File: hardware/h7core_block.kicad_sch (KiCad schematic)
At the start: 71 parts, among them J1 USB-C, J3 TC2030-NL SWD, U1 STM32H743VIT6, U3 AP63203WU-7, U4 TLV75533PDBVR, U6 PCM5102APWR, U8 PCM1808PWR, Y1 25MHz 12pF

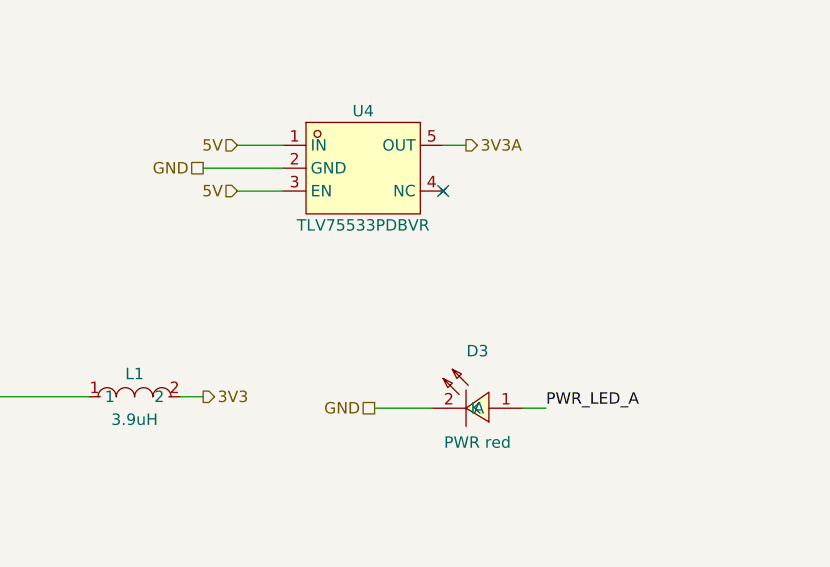
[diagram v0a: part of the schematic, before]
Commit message: feat(sch): add SP809 3V3 supervisor gating TLV75533 EN
U107 SP809EK-L-2-9 (push-pull active-low, 2.9 V, 140 ms min) drives TLV75533 EN on new net LDO_EN, replacing the 5V tie, so 3V3A comes up only after 3V3 is valid. C166 100 nF at its VCC. No pull-up: the output is push-pull.
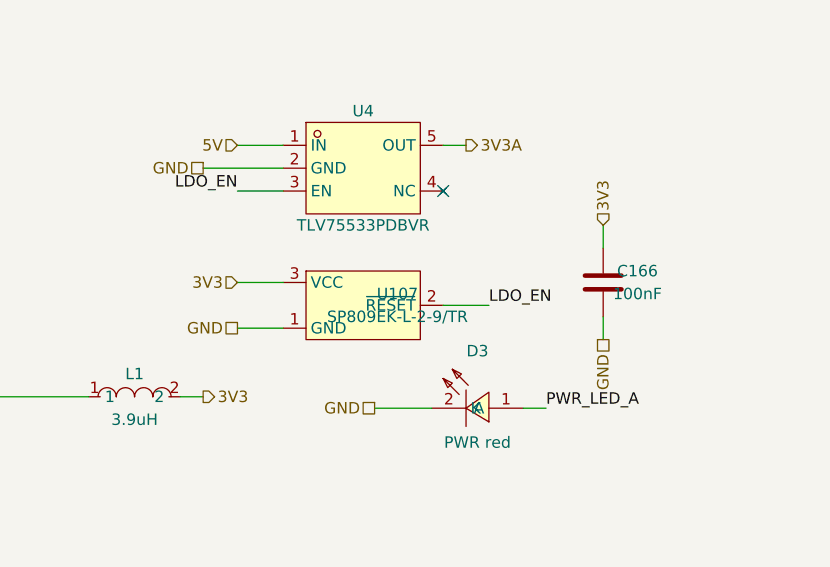
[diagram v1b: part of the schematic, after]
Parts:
- added C166: 100nF, Capacitor_SMD:C_0402_1005Metric, symbol Device:C
- added U107: SP809EK-L-2-9/TR, Package_TO_SOT_SMD:SOT-23, symbol cubevox_h7core:SP809EK-L-2-9
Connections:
- net 3V3: now also C166.1, U107.3 (VCC)
- net 5V: no longer U4.3 (EN)
- net GND: now also C166.2, U107.1 (GND)
- new net LDO_EN: U107.2 (~{RESET}), U4.3 (EN)
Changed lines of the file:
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@@
 		)
 	)
-	(hierarchical_label "5V"
-		(shape input)
+	(label "LDO_EN"
 		(at 284.48 104.14 180)
 		(fields_autoplaced yes)
@@
 		)
 	)
+	(symbol
+		(lib_id "cubevox_h7core:SP809EK-L-2-9")
+		(at 298.45 116.84 0)
+		(unit 1)
+		(exclude_from_sim no)
+		(in_bom yes)
+		(on_board yes)
+		(dnp no)
+		(property "Reference" "U107"
+			(at 302.26 115.57000000000001 0)
+			(effects
+				(font
+					(size 1.27 1.27)
+				)
+			)
+		)
+		(property "Value" "SP809EK-L-2-9/TR"
+			(at 302.26 118.11 0)
+			(effects
+				(font
+					(size 1.27 1.27)
+				)
+			)
+		)
+		(property "Footprint" "Package_TO_SOT_SMD:SOT-23"
+			(at 298.45 116.84 0)
+			(hide yes)
+			(effects
+				(font
+					(size 1.27 1.27)
+				)
+			)
+		)
+		(property "Datasheet" "~"
+			(at 298.45 116.84 0)
+			(hide yes)
+			(effects
+				(font
+					(size 1.27 1.27)
+				)
+			)
+		)
+		(property "LCSC" "C412495"
+			(at 298.45 116.84 0)
+			(hide yes)
+			(effects
+				(font
+					(size 1.27 1.27)
+				)
+			)
+		)
+		(property "MPN" "SP809EK-L-2-9/TR"
+			(at 298.45 116.84 0)
+			(hide yes)
+			(effects
+				(font
+					(size 1.27 1.27)
+				)
+			)
+		)
+		(pin "1"
+		)
+		(pin "2"
+		)
+		(pin "3"
+		)
+		(instances
+			(project "cubevox"
+				(path "/99ad1494-2bf8-5051-8886-2c8b83c86254/cdf9c81d-d554-530c-ae51-0929232e7fb3"
+					(reference "U107")
+					(unit 1)
+				)
+			)
+		)
+	)
+	(wire
+		(pts
+			(xy 289.56 114.3) (xy 284.48 114.3)
+		)
+		(stroke
+			(width 0)
+			(type default)
+		)
+	)
+	(hierarchical_label "3V3"
+		(shape input)
+		(at 284.48 114.3 180)
+		(fields_autoplaced yes)
+		(effects
+			(font
+				(size 1.27 1.27)
+			)
+			(justify right bottom)
+		)
+	)
+	(wire
+		(pts
+			(xy 289.56 119.38) (xy 284.48 119.38)
+		)
+		(stroke
+			(width 0)
+			(type default)
+		)
+	)
+	(hierarchical_label "GND"
+		(shape passive)
+		(at 284.48 119.38 180)
+		(fields_autoplaced yes)
+		(effects
+			(font
+				(size 1.27 1.27)
+			)
+			(justify right bottom)
+		)
+	)
+	(wire
+		(pts
+			(xy 307.34 116.84) (xy 312.42 116.84)
+		)
+		(stroke
+			(width 0)
+			(type default)
+		)
+	)
+	(label "LDO_EN"
+		(at 312.42 116.84 0)
+		(fields_autoplaced yes)
+		(effects
+			(font
+				(size 1.27 1.27)
+			)
+			(justify left bottom)
+		)
+	)
+	(symbol
+		(lib_id "Device:C")
+		(at 325.12 114.3 0)
+		(unit 1)
+		(exclude_from_sim no)
+		(in_bom yes)
+		(on_board yes)
+		(dnp no)
+		(property "Reference" "C166"
+			(at 328.93 113.03 0)
+			(effects
+				(font
+					(size 1.27 1.27)
+				)
+			)
+		)
+		(property "Value" "100nF"
+			(at 328.93 115.57 0)
+			(effects
+				(font
+					(size 1.27 1.27)
+				)
+			)
+		)
+		(property "Footprint" "Capacitor_SMD:C_0402_1005Metric"
+			(at 325.12 114.3 0)
+			(hide yes)
+			(effects
+				(font
+					(size 1.27 1.27)
+				)
+			)
+		)
+		(property "Datasheet" "~"
+			(at 325.12 114.3 0)
+			(hide yes)
+			(effects
+				(font
+					(size 1.27 1.27)
+				)
+			)
+		)
+		(property "LCSC" "C1525"
+			(at 325.12 114.3 0)
+			(hide yes)
+			(effects
+				(font
+					(size 1.27 1.27)
+				)
+			)
+		)
+		(pin "1"
+		)
+		(pin "2"
+		)
+		(instances
+			(project "cubevox"
+				(path "/99ad1494-2bf8-5051-8886-2c8b83c86254/cdf9c81d-d554-530c-ae51-0929232e7fb3"
+					(reference "C166")
+					(unit 1)
+				)
+			)
+		)
+	)
+	(wire
+		(pts
+			(xy 325.12 110.49) (xy 325.12 107.95)
+		)
+		(stroke
+			(width 0)
+			(type default)
+		)
+	)
+	(hierarchical_label "3V3"
+		(shape input)
+		(at 325.12 107.95 90)
+		(fields_autoplaced yes)
+		(effects
+			(font
+				(size 1.27 1.27)
+			)
+			(justify left bottom)
+		)
+	)
+	(wire
+		(pts
+			(xy 325.12 118.11) (xy 325.12 120.64999999999999)
+		)
+		(stroke
+			(width 0)
+			(type default)
+		)
+	)
+	(hierarchical_label "GND"
+		(shape passive)
+		(at 325.12 120.64999999999999 270)
+		(fields_autoplaced yes)
+		(effects
+			(font
+				(size 1.27 1.27)
+			)
+			(justify right bottom)
+		)
+	)

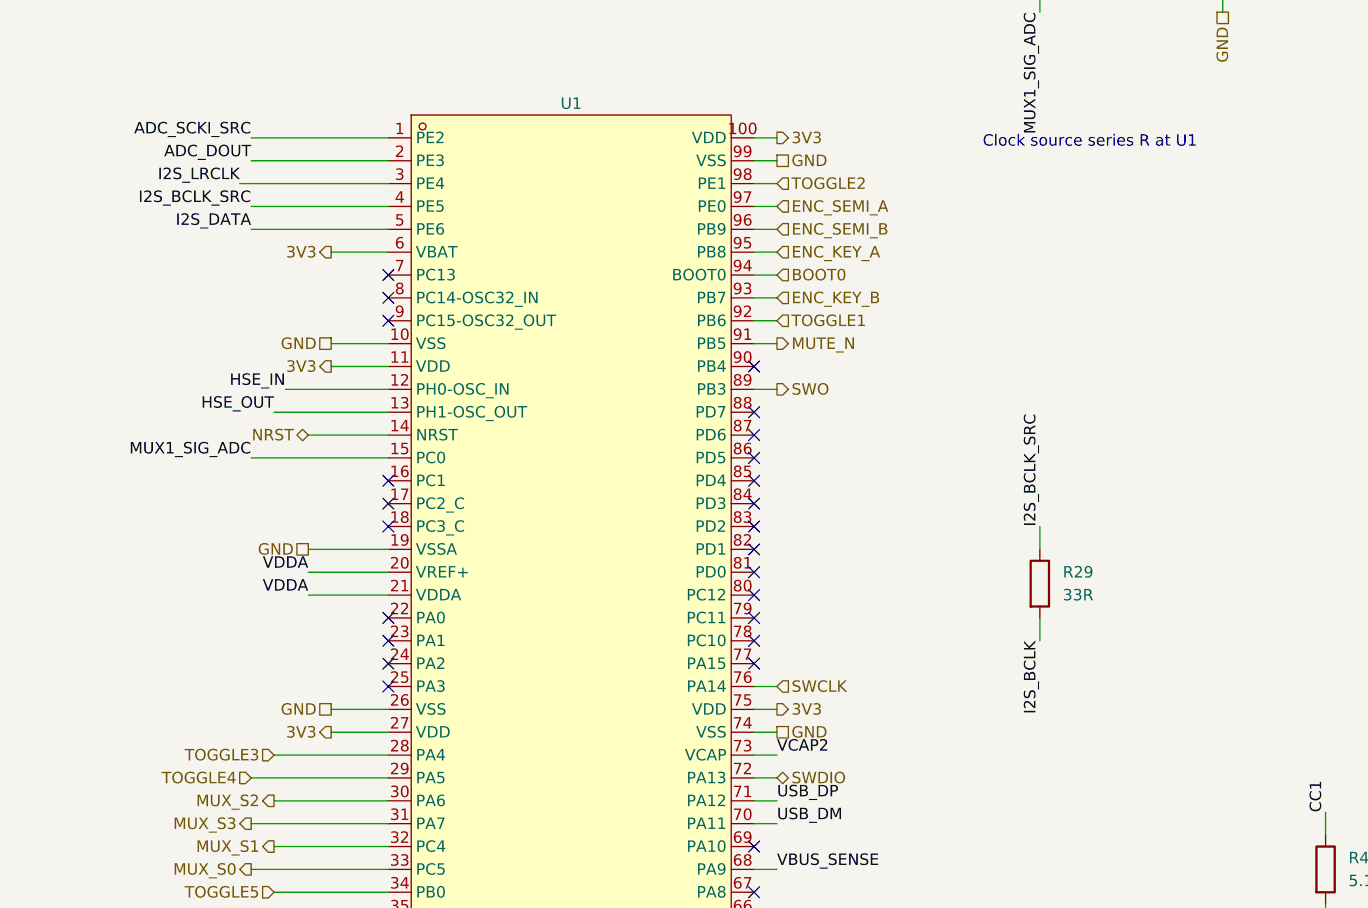
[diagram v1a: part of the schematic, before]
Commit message: feat(sch): add 33R series resistors on I2S at U1
R156 (LRCLK) and R157 (DATA), 33R 0402 (LCSC C25105), sit at the U1 escapes like R29 on BCLK, so each I2S line leaves the MCU through a source resistor. U1 sides become I2S_LRCLK_SRC and I2S_DATA_SRC. ERC: no new violations.
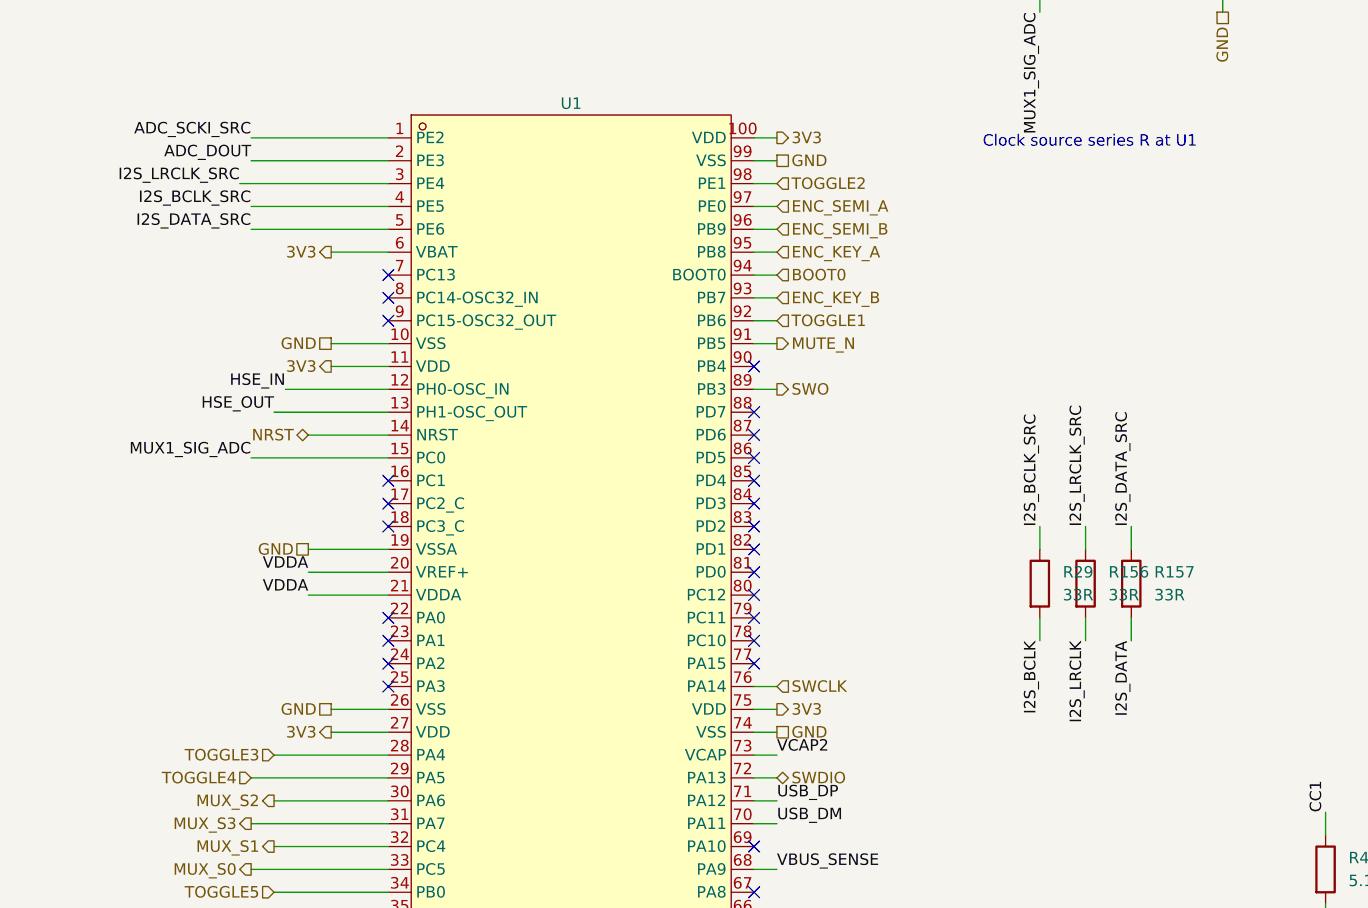
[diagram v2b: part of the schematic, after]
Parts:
- added R156, R157: 33R, Resistor_SMD:R_0402_1005Metric, symbol Device:R
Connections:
- net I2S_DATA: now also R157.2; no longer U1.5 (PE6)
- net I2S_LRCLK: now also R156.2; no longer U1.3 (PE4)
- new net I2S_DATA_SRC: R157.1, U1.5 (PE6)
- new net I2S_LRCLK_SRC: R156.1, U1.3 (PE4)
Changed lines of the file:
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@@
 		)
 	)
-	(label "I2S_LRCLK"
+	(label "I2S_LRCLK_SRC"
 		(at 38.1 82.55 180)
 		(fields_autoplaced yes)
@@
 		)
 	)
-	(label "I2S_DATA"
+	(label "I2S_DATA_SRC"
 		(at 39.37 87.63 180)
 		(fields_autoplaced yes)
@@
 		(fields_autoplaced yes)
 		(effects
+			(font
+				(size 1.27 1.27)
+			)
+			(justify right bottom)
+		)
+	)
+	(symbol
+		(lib_id "Device:R")
+		(at 132.08 127 0)
+		(unit 1)
+		(exclude_from_sim no)
+		(in_bom yes)
+		(on_board yes)
+		(dnp no)
+		(property "Reference" "R156"
+			(at 134.62 125.73 0)
+			(effects
+				(font
+					(size 1.27 1.27)
+				)
+				(justify left)
+			)
+		)
+		(property "Value" "33R"
+			(at 134.62 128.27 0)
+			(effects
+				(font
+					(size 1.27 1.27)
+				)
+				(justify left)
+			)
+		)
+		(property "Footprint" "Resistor_SMD:R_0402_1005Metric"
+			(at 132.08 127 0)
+			(hide yes)
+			(effects
+				(font
+					(size 1.27 1.27)
+				)
+			)
+		)
+		(property "Datasheet" "~"
+			(at 132.08 127 0)
+			(hide yes)
+			(effects
+				(font
+					(size 1.27 1.27)
+				)
+			)
+		)
+		(property "LCSC" "C25105"
+			(at 132.08 127 0)
+			(hide yes)
+			(effects
+				(font
+					(size 1.27 1.27)
+				)
+			)
+		)
+		(pin "1"
+		)
+		(pin "2"
+		)
+		(instances
+			(project "cubevox"
+				(path "/99ad1494-2bf8-5051-8886-2c8b83c86254/cdf9c81d-d554-530c-ae51-0929232e7fb3"
+					(reference "R156")
+					(unit 1)
+				)
+			)
+		)
+	)
+	(wire
+		(pts
+			(xy 132.08 123.19) (xy 132.08 120.65)
+		)
+		(stroke
+			(width 0)
+			(type default)
+		)
+	)
+	(label "I2S_LRCLK_SRC"
+		(at 132.08 120.65 90)
+		(fields_autoplaced yes)
+		(effects
+			(font
+				(size 1.27 1.27)
+			)
+			(justify left bottom)
+		)
+	)
+	(wire
+		(pts
+			(xy 132.08 130.81) (xy 132.08 133.35)
+		)
+		(stroke
+			(width 0)
+			(type default)
+		)
+	)
+	(label "I2S_LRCLK"
+		(at 132.08 133.35 270)
+		(fields_autoplaced yes)
+		(effects
+			(font
+				(size 1.27 1.27)
+			)
+			(justify right bottom)
+		)
+	)
+	(symbol
+		(lib_id "Device:R")
+		(at 137.16 127 0)
+		(unit 1)
+		(exclude_from_sim no)
+		(in_bom yes)
+		(on_board yes)
+		(dnp no)
+		(property "Reference" "R157"
+			(at 139.7 125.73 0)
+			(effects
+				(font
+					(size 1.27 1.27)
+				)
+				(justify left)
+			)
+		)
+		(property "Value" "33R"
+			(at 139.7 128.27 0)
+			(effects
+				(font
+					(size 1.27 1.27)
+				)
+				(justify left)
+			)
+		)
+		(property "Footprint" "Resistor_SMD:R_0402_1005Metric"
+			(at 137.16 127 0)
+			(hide yes)
+			(effects
+				(font
+					(size 1.27 1.27)
+				)
+			)
+		)
+		(property "Datasheet" "~"
+			(at 137.16 127 0)
+			(hide yes)
+			(effects
+				(font
+					(size 1.27 1.27)
+				)
+			)
+		)
+		(property "LCSC" "C25105"
+			(at 137.16 127 0)
+			(hide yes)
+			(effects
+				(font
+					(size 1.27 1.27)
+				)
+			)
+		)
+		(pin "1"
+		)
+		(pin "2"
+		)
+		(instances
+			(project "cubevox"
+				(path "/99ad1494-2bf8-5051-8886-2c8b83c86254/cdf9c81d-d554-530c-ae51-0929232e7fb3"
+					(reference "R157")
+					(unit 1)
+				)
+			)
+		)
+	)
+	(wire
+		(pts
+			(xy 137.16 123.19) (xy 137.16 120.65)
+		)
+		(stroke
+			(width 0)
+			(type default)
+		)
+	)
+	(label "I2S_DATA_SRC"
+		(at 137.16 120.65 90)
+		(fields_autoplaced yes)
+		(effects
+			(font
+				(size 1.27 1.27)
+			)
+			(justify left bottom)
+		)
+	)
+	(wire
+		(pts
+			(xy 137.16 130.81) (xy 137.16 133.35)
+		)
+		(stroke
+			(width 0)
+			(type default)
+		)
+	)
+	(label "I2S_DATA"
+		(at 137.16 133.35 270)
+		(fields_autoplaced yes)
+		(effects

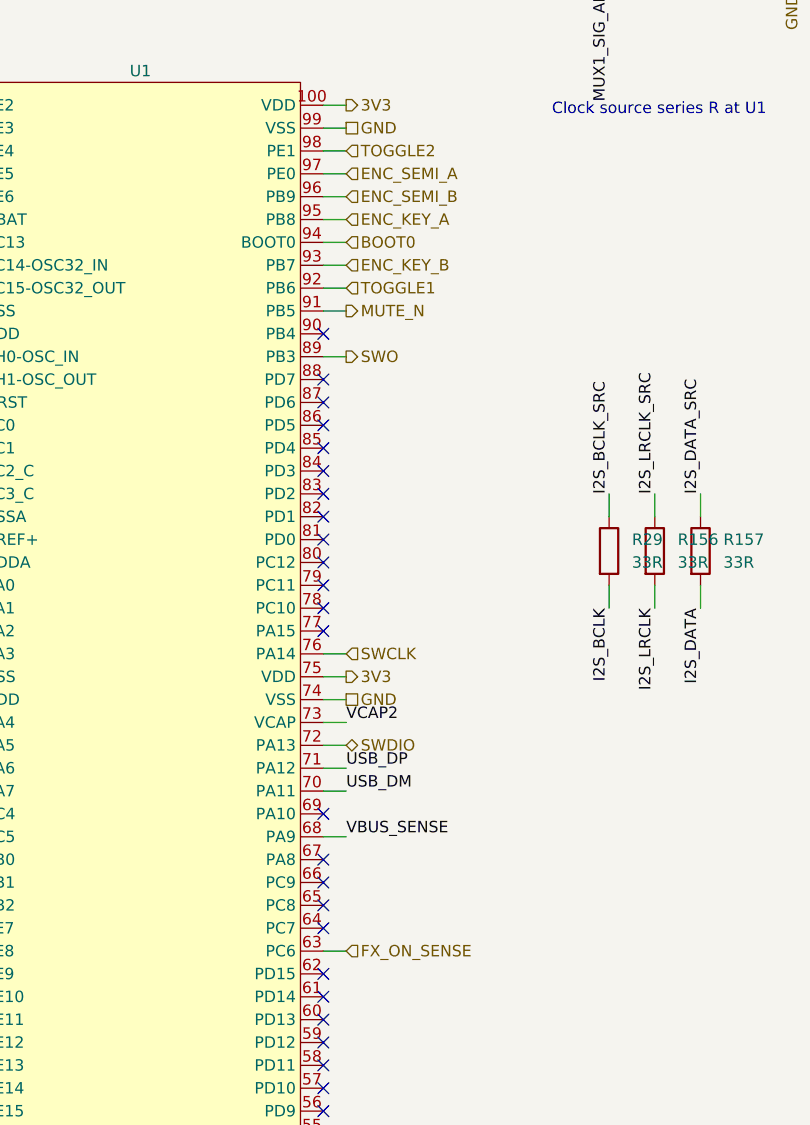
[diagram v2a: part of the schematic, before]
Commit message: feat(sch): slots revision, KEY/SEMITONES pots, bypass relay out, MUTE_SW
ENC102/ENC103 and their debounce RC (R130-R133, C146-C149) become pots
RV115/RV116 on U101 I14/I15 (POT15/POT16). K101, D104 and the PRE_OUT dry
path leave, DAC_ATT joins BUF_IN. SWBYPASS1 now drives MUTE_SW (the former
FX_ON_SENSE); PB7, PB8, PB9, PE0 are no-connect. ERC: 0 errors.
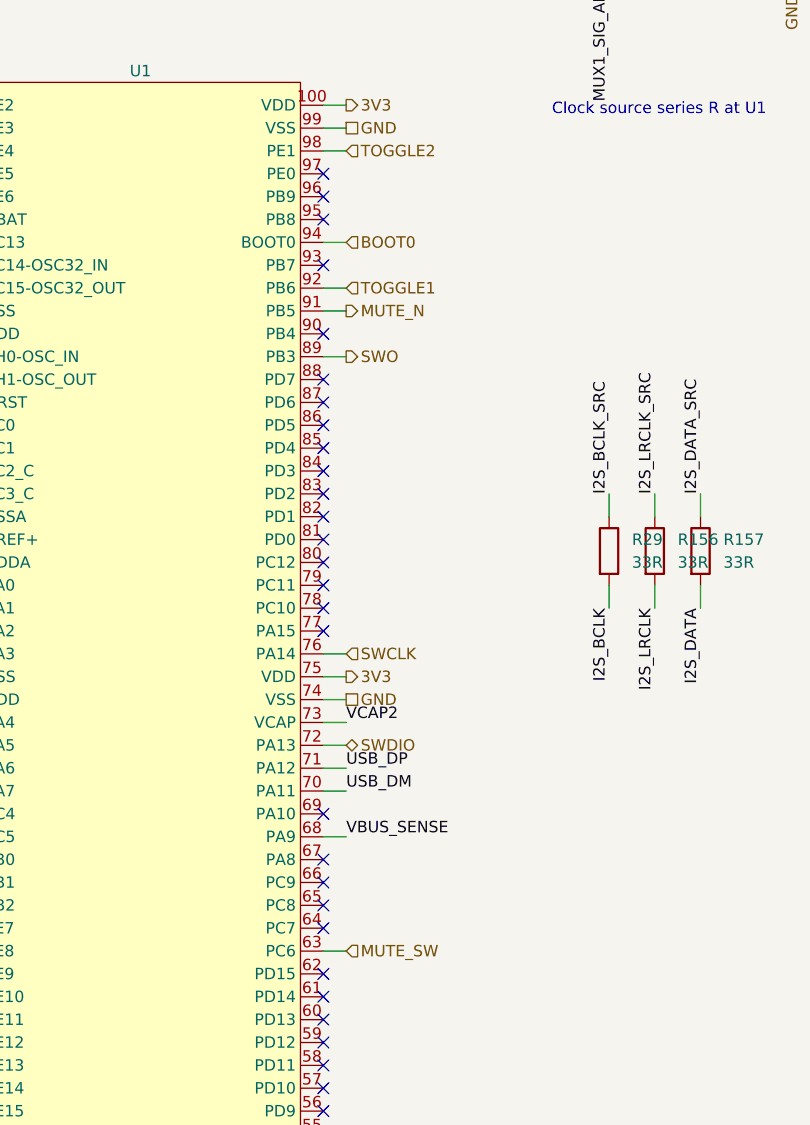
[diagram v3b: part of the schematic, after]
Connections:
- net ENC_KEY_A: no longer names the net of U1.95 (PB8)
- net ENC_KEY_B: no longer names the net of U1.93 (PB7)
- net ENC_SEMI_A: no longer names the net of U1.97 (PE0)
- net ENC_SEMI_B: no longer names the net of U1.96 (PB9)
- net FX_ON_SENSE renamed MUTE_SW
- no-connect marks 46 -> 50
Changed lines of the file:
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@@
 		)
 	)
-	(hierarchical_label "FX_ON_SENSE"
+	(hierarchical_label "MUTE_SW"
 		(shape input)
 		(at 97.79 171.45 0)
@@
 	(wire
 		(pts
-			(xy 95.25 95.25) (xy 97.79 95.25)
-		)
-		(stroke
-			(width 0)
-			(type default)
-		)
-	)
-	(hierarchical_label "ENC_KEY_B"
-		(shape input)
-		(at 97.79 95.25 0)
-		(fields_autoplaced yes)
-		(effects
-			(font
-				(size 1.27 1.27)
-			)
-			(justify left bottom)
-		)
-	)
-	(wire
-		(pts
 			(xy 95.25 92.71) (xy 97.79 92.71)
 		)
@@
 	(wire
 		(pts
-			(xy 95.25 90.17) (xy 97.79 90.17)
-		)
-		(stroke
-			(width 0)
-			(type default)
-		)
-	)
-	(hierarchical_label "ENC_KEY_A"
-		(shape input)
-		(at 97.79 90.17 0)
-		(fields_autoplaced yes)
-		(effects
-			(font
-				(size 1.27 1.27)
-			)
-			(justify left bottom)
-		)
-	)
-	(wire
-		(pts
-			(xy 95.25 87.63) (xy 97.79 87.63)
-		)
-		(stroke
-			(width 0)
-			(type default)
-		)
-	)
-	(hierarchical_label "ENC_SEMI_B"
-		(shape input)
-		(at 97.79 87.63 0)
-		(fields_autoplaced yes)
-		(effects
-			(font
-				(size 1.27 1.27)
-			)
-			(justify left bottom)
-		)
-	)
-	(wire
-		(pts
-			(xy 95.25 85.09) (xy 97.79 85.09)
-		)
-		(stroke
-			(width 0)
-			(type default)
-		)
-	)
-	(hierarchical_label "ENC_SEMI_A"
-		(shape input)
-		(at 97.79 85.09 0)
-		(fields_autoplaced yes)
-		(effects
-			(font
-				(size 1.27 1.27)
-			)
-			(justify left bottom)
-		)
-	)
-	(wire
-		(pts
 			(xy 95.25 82.55) (xy 97.79 82.55)
 		)
@@
 		)
 	)
+	(no_connect
+		(at 95.25 95.25)
+	)
+	(no_connect
+		(at 95.25 90.17)
+	)
+	(no_connect
+		(at 95.25 87.63)
+	)
+	(no_connect
+		(at 95.25 85.09)
+	)
 	(sheet_instances
